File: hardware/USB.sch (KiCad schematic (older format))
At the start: 9 parts, among them IC9 FT232RL, J2 USB_A

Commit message: Working on layout
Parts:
- D11: value Tx -> TX
- D12: value Rx -> RX
- J2: value USB_A -> SERIAL; Mfr. (none) -> Wurth Elektronik; Mfr. No. (none) -> 629105150521; Mouser (none) -> 710-629105150521
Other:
- moved on the sheet: D11, D12, R6, R7
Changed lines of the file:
@@
 EESchema Schematic File Version 4
-LIBS:Sweet 6502 Computer-cache
+LIBS:Retro PC-cache
 EELAYER 30 0
 EELAYER END
@@
 AR Path="/5E9064F2/5E95D1DF" Ref="J2"  Part="1"
 F 0 "J2" H 2970 3347 50  0000 R CNN
-F 1 "USB_A" H 2970 3438 50  0000 R CNN
+F 1 "SERIAL" H 2970 3438 50  0000 R CNN
 F 2 "Connector_USB:USB_Micro-B_Wuerth_629105150521" H 3350 3400 50  0001 C CNN
 F 3 "https://www.belfuse.com/resources/datasheets/stewartconnector/ds-stw-usb-2.0-and-3.0-connectors.pdf" H 3350 3400 50  0001 C CNN
-F 4 "" H 3200 3450 50  0001 C CNN "Mfr."
-F 5 "" H 3200 3450 50  0001 C CNN "Mfr. No."
-F 6 "" H 3200 3450 50  0001 C CNN "Mouser"
+F 4 "Wurth Elektronik" H 3200 3450 50  0001 C CNN "Mfr."
+F 5 "629105150521" H 3200 3450 50  0001 C CNN "Mfr. No."
+F 6 "710-629105150521" H 3200 3450 50  0001 C CNN "Mouser"
 	1    3200 3450
 	1    0    0    -1
@@
 L Device:LED D?
 U 1 1 5E95D1E6
-P 7400 3950
+P 7400 3500
 AR Path="/5E95D1E6" Ref="D?"  Part="1"
 AR Path="/5E9064F2/5E95D1E6" Ref="D11"  Part="1"
-F 0 "D11" V 7439 3832 50  0000 R CNN
-F 1 "Tx" V 7348 3832 50  0000 R CNN
-F 2 "LED_SMD:LED_0805_2012Metric" H 7400 3950 50  0001 C CNN
-F 3 "https://www.mouser.de/datasheet/2/216/apt2012pyw-1173287.pdf" H 7400 3950 50  0001 C CNN
-F 4 "Kingbright" H 7400 3950 50  0001 C CNN "Mfr."
-F 5 "APT2012PYW" H 7400 3950 50  0001 C CNN "Mfr. No."
-F 6 "604-APT2012PYW" H 7400 3950 50  0001 C CNN "Mouser"
-	1    7400 3950
+F 0 "D11" V 7439 3382 50  0000 R CNN
+F 1 "TX" V 7348 3382 50  0000 R CNN
+F 2 "LED_SMD:LED_0805_2012Metric" H 7400 3500 50  0001 C CNN
+F 3 "https://www.mouser.de/datasheet/2/216/apt2012pyw-1173287.pdf" H 7400 3500 50  0001 C CNN
+F 4 "Kingbright" H 7400 3500 50  0001 C CNN "Mfr."
+F 5 "APT2012PYW" H 7400 3500 50  0001 C CNN "Mfr. No."
+F 6 "604-APT2012PYW" H 7400 3500 50  0001 C CNN "Mouser"
+	1    7400 3500
 	0    -1   -1   0
 $EndComp
@@
 L Device:R R?
 U 1 1 5E95D1EC
-P 7400 3600
+P 7400 3950
 AR Path="/5E95D1EC" Ref="R?"  Part="1"
 AR Path="/5E9064F2/5E95D1EC" Ref="R6"  Part="1"
-F 0 "R6" H 7470 3646 50  0000 L CNN
-F 1 "1k" H 7470 3555 50  0000 L CNN
-F 2 "Resistor_SMD:R_0805_2012Metric" V 7330 3600 50  0001 C CNN
-F 3 "~" H 7400 3600 50  0001 C CNN
-F 4 "Vishay / Dale" H 7400 3600 50  0001 C CNN "Mfr."
-F 5 "CRCW08051K00FKEAC" H 7400 3600 50  0001 C CNN "Mfr. No."
-F 6 "71-CRCW08051K00FKEAC" H 7400 3600 50  0001 C CNN "Mouser"
-	1    7400 3600
+F 0 "R6" H 7470 3996 50  0000 L CNN
+F 1 "1k" H 7470 3905 50  0000 L CNN
+F 2 "Resistor_SMD:R_0805_2012Metric" V 7330 3950 50  0001 C CNN
+F 3 "https://www.mouser.de/datasheet/2/427/crcwce3-1223726.pdf" H 7400 3950 50  0001 C CNN
+F 4 "Vishay / Dale" H 7400 3950 50  0001 C CNN "Mfr."
+F 5 "CRCW08051K00FKEAC" H 7400 3950 50  0001 C CNN "Mfr. No."
+F 6 "71-CRCW08051K00FKEAC" H 7400 3950 50  0001 C CNN "Mouser"
+	1    7400 3950
 	1    0    0    -1
 $EndComp
@@
 L Device:R R?
 U 1 1 5E95D1F2
-P 7750 3600
+P 7750 3950
 AR Path="/5E95D1F2" Ref="R?"  Part="1"
 AR Path="/5E9064F2/5E95D1F2" Ref="R7"  Part="1"
-F 0 "R7" H 7820 3646 50  0000 L CNN
-F 1 "1k" H 7820 3555 50  0000 L CNN
-F 2 "Resistor_SMD:R_0805_2012Metric" V 7680 3600 50  0001 C CNN
-F 3 "~" H 7750 3600 50  0001 C CNN
-F 4 "Vishay / Dale" H 7750 3600 50  0001 C CNN "Mfr."
-F 5 "CRCW08051K00FKEAC" H 7750 3600 50  0001 C CNN "Mfr. No."
-F 6 "71-CRCW08051K00FKEAC" H 7750 3600 50  0001 C CNN "Mouser"
-	1    7750 3600
+F 0 "R7" H 7820 3996 50  0000 L CNN
+F 1 "1k" H 7820 3905 50  0000 L CNN
+F 2 "Resistor_SMD:R_0805_2012Metric" V 7680 3950 50  0001 C CNN
+F 3 "https://www.mouser.de/datasheet/2/427/crcwce3-1223726.pdf" H 7750 3950 50  0001 C CNN
+F 4 "Vishay / Dale" H 7750 3950 50  0001 C CNN "Mfr."
+F 5 "CRCW08051K00FKEAC" H 7750 3950 50  0001 C CNN "Mfr. No."
+F 6 "71-CRCW08051K00FKEAC" H 7750 3950 50  0001 C CNN "Mouser"
+	1    7750 3950
 	1    0    0    -1
 $EndComp
@@
 L Device:LED D?
 U 1 1 5E95D1F8
-P 7750 3950
+P 7750 3500
 AR Path="/5E95D1F8" Ref="D?"  Part="1"
 AR Path="/5E9064F2/5E95D1F8" Ref="D12"  Part="1"
-F 0 "D12" V 7789 3832 50  0000 R CNN
-F 1 "Rx" V 7698 3832 50  0000 R CNN
-F 2 "LED_SMD:LED_0805_2012Metric" H 7750 3950 50  0001 C CNN
-F 3 "https://www.mouser.de/datasheet/2/216/apt2012pgw-1173286.pdf" H 7750 3950 50  0001 C CNN
-F 4 "Kingbright" H 7750 3950 50  0001 C CNN "Mfr."
-F 5 "APT2012PGW" H 7750 3950 50  0001 C CNN "Mfr. No."
-F 6 "604-APT2012PGW" H 7750 3950 50  0001 C CNN "Mouser"
-	1    7750 3950
+F 0 "D12" V 7789 3382 50  0000 R CNN
+F 1 "RX" V 7698 3382 50  0000 R CNN
+F 2 "LED_SMD:LED_0805_2012Metric" H 7750 3500 50  0001 C CNN
+F 3 "https://www.mouser.de/datasheet/2/216/apt2012pgw-1173286.pdf" H 7750 3500 50  0001 C CNN
+F 4 "Kingbright" H 7750 3500 50  0001 C CNN "Mfr."
+F 5 "APT2012PGW" H 7750 3500 50  0001 C CNN "Mfr. No."
+F 6 "604-APT2012PGW" H 7750 3500 50  0001 C CNN "Mouser"
+	1    7750 3500
 	0    -1   -1   0
 $EndComp
@@
 F 1 "100nF" H 4515 3105 50  0000 L CNN
 F 2 "Capacitor_SMD:C_0805_2012Metric" H 4438 3000 50  0001 C CNN
-F 3 "~" H 4400 3150 50  0001 C CNN
+F 3 "https://www.mouser.de/datasheet/2/212/KEM_C1002_X7R_SMD-1102033.pdf" H 4400 3150 50  0001 C CNN
 F 4 "KEMET" H 4400 3150 50  0001 C CNN "Mfr."
 F 5 "C0805C104K5RACTU" H 4400 3150 50  0001 C CNN "Mfr. No."
@@
 	7600 3300 7400 3300
 Wire Wire Line
-	7400 3300 7400 3450
-Wire Wire Line
 	7600 3300 7750 3300
-Wire Wire Line
-	7750 3300 7750 3450
 Connection ~ 7600 3300
 Wire Wire Line
-	7750 3750 7750 3800
-Wire Wire Line
-	7400 3750 7400 3800
-Wire Wire Line
 	6450 4150 7400 4150
 Wire Wire Line
-	7400 4150 7400 4100
-Wire Wire Line
 	6450 4250 7750 4250
 Wire Wire Line
-	7750 4250 7750 4100
+	7750 3800 7750 3650
 Wire Wire Line
 	4750 3850 4850 3850
@@
 F 1 "100nF" H 5265 2355 50  0000 L CNN
 F 2 "Capacitor_SMD:C_0805_2012Metric" H 5188 2250 50  0001 C CNN
-F 3 "~" H 5150 2400 50  0001 C CNN
+F 3 "https://www.mouser.de/datasheet/2/212/KEM_C1002_X7R_SMD-1102033.pdf" H 5150 2400 50  0001 C CNN
 F 4 "KEMET" H 5150 2400 50  0001 C CNN "Mfr."
 F 5 "C0805C104K5RACTU" H 5150 2400 50  0001 C CNN "Mfr. No."
@@
 F 1 "100nF" H 6065 2355 50  0000 L CNN
 F 2 "Capacitor_SMD:C_0805_2012Metric" H 5988 2250 50  0001 C CNN
-F 3 "~" H 5950 2400 50  0001 C CNN
+F 3 "https://www.mouser.de/datasheet/2/212/KEM_C1002_X7R_SMD-1102033.pdf" H 5950 2400 50  0001 C CNN
 F 4 "KEMET" H 5950 2400 50  0001 C CNN "Mfr."
 F 5 "C0805C104K5RACTU" H 5950 2400 50  0001 C CNN "Mfr. No."
@@
 	5750 2000 5750 2100
 Connection ~ 5750 2100
+Wire Wire Line
+	7400 4100 7400 4150
+Wire Wire Line
+	7750 4100 7750 4250
+Wire Wire Line
+	7400 3650 7400 3800
+Wire Wire Line
+	7400 3350 7400 3300
+Wire Wire Line
+	7750 3350 7750 3300
 $EndSCHEMATC

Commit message: Working on layout
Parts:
- J2: footprint Connector_USB:USB_Micro-B_Wuerth_629105150521 -> Connector_USB:USB_B_TE_5787834_Vertical; Mfr. Wurth Elektronik -> TE Connectivity; Mfr. No. 629105150521 -> 5787834-1; Mouser 710-629105150521 -> 571-5787834-1
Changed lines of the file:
@@
 $Descr A4 11693 8268
 encoding utf-8
-Sheet 4 6
+Sheet 3 6
 Title "Retro PC"
 Date "2019-10-08"
@@
 F 0 "J2" H 2970 3347 50  0000 R CNN
 F 1 "SERIAL" H 2970 3438 50  0000 R CNN
-F 2 "Connector_USB:USB_Micro-B_Wuerth_629105150521" H 3350 3400 50  0001 C CNN
+F 2 "Connector_USB:USB_B_TE_5787834_Vertical" H 3350 3400 50  0001 C CNN
 F 3 "https://www.belfuse.com/resources/datasheets/stewartconnector/ds-stw-usb-2.0-and-3.0-connectors.pdf" H 3350 3400 50  0001 C CNN
-F 4 "Wurth Elektronik" H 3200 3450 50  0001 C CNN "Mfr."
-F 5 "629105150521" H 3200 3450 50  0001 C CNN "Mfr. No."
-F 6 "710-629105150521" H 3200 3450 50  0001 C CNN "Mouser"
+F 4 "TE Connectivity" H 3200 3450 50  0001 C CNN "Mfr."
+F 5 "5787834-1" H 3200 3450 50  0001 C CNN "Mfr. No."
+F 6 "571-5787834-1" H 3200 3450 50  0001 C CNN "Mouser"
 	1    3200 3450
 	1    0    0    -1

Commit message: Working on layout
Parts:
- J2: footprint Connector_USB:USB_B_TE_5787834_Vertical -> TE_Connectivity:USB_B_TE_2923042_Horizontal; Mfr. No. 5787834-1 -> 292304-2; Mouser 571-5787834-1 -> 571-292304-2
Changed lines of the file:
@@
 F 0 "J2" H 2970 3347 50  0000 R CNN
 F 1 "SERIAL" H 2970 3438 50  0000 R CNN
-F 2 "Connector_USB:USB_B_TE_5787834_Vertical" H 3350 3400 50  0001 C CNN
-F 3 "https://www.belfuse.com/resources/datasheets/stewartconnector/ds-stw-usb-2.0-and-3.0-connectors.pdf" H 3350 3400 50  0001 C CNN
+F 2 "TE_Connectivity:USB_B_TE_2923042_Horizontal" H 3350 3400 50  0001 C CNN
+F 3 "https://www.te.com/commerce/DocumentDelivery/DDEController?Action=showdoc&DocId=Customer+Drawing%7F292304%7FD4%7Fpdf%7FEnglish%7FENG_CD_292304_D4.pdf%7F292304-2" H 3350 3400 50  0001 C CNN
 F 4 "TE Connectivity" H 3200 3450 50  0001 C CNN "Mfr."
-F 5 "5787834-1" H 3200 3450 50  0001 C CNN "Mfr. No."
-F 6 "571-5787834-1" H 3200 3450 50  0001 C CNN "Mouser"
+F 5 "292304-2" H 3200 3450 50  0001 C CNN "Mfr. No."
+F 6 "571-292304-2" H 3200 3450 50  0001 C CNN "Mouser"
 	1    3200 3450
 	1    0    0    -1

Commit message: Working on layout
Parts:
- removed J2: SERIAL, TE_Connectivity:USB_B_TE_2923042_Horizontal, symbol Connector:USB_A
- added J1: USB_B, TE_Connectivity:USB_B_TE_2923042_Horizontal, symbol TE_Connectivity:USB_B
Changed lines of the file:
@@
-$EndComp
-$Comp
-L Connector:USB_A J?
-U 1 1 5E95D1DF
-P 3200 3450
-AR Path="/5E95D1DF" Ref="J?"  Part="1"
-AR Path="/5E9064F2/5E95D1DF" Ref="J2"  Part="1"
-F 0 "J2" H 2970 3347 50  0000 R CNN
-F 1 "SERIAL" H 2970 3438 50  0000 R CNN
-F 2 "TE_Connectivity:USB_B_TE_2923042_Horizontal" H 3350 3400 50  0001 C CNN
-F 3 "https://www.te.com/commerce/DocumentDelivery/DDEController?Action=showdoc&DocId=Customer+Drawing%7F292304%7FD4%7Fpdf%7FEnglish%7FENG_CD_292304_D4.pdf%7F292304-2" H 3350 3400 50  0001 C CNN
-F 4 "TE Connectivity" H 3200 3450 50  0001 C CNN "Mfr."
-F 5 "292304-2" H 3200 3450 50  0001 C CNN "Mfr. No."
-F 6 "571-292304-2" H 3200 3450 50  0001 C CNN "Mouser"
-	1    3200 3450
-	1    0    0    -1
 $EndComp
 $Comp
@@
 Wire Wire Line
 	7750 3350 7750 3300
+$Comp
+L TE_Connectivity:USB_B J1
+U 1 1 5DA7E5BF
+P 3200 3450
+F 0 "J1" H 3257 3917 50  0000 C CNN
+F 1 "USB_B" H 3257 3826 50  0000 C CNN
+F 2 "TE_Connectivity:USB_B_TE_2923042_Horizontal" H 3350 3400 50  0001 C CNN
+F 3 "https://www.te.com/commerce/DocumentDelivery/DDEController?Action=showdoc&DocId=Customer+Drawing%7F292304%7FD4%7Fpdf%7FEnglish%7FENG_CD_292304_D4.pdf%7F292304-2" H 3350 3400 50  0001 C CNN
+F 4 "TE Connectivity" H 3257 4007 50  0001 C CNN "Mfr."
+F 5 "292304-2" H 3257 3916 50  0001 C CNN "Mfr. No."
+F 6 "571-292304-2" H 3257 3825 50  0001 C CNN "Mouser"
+	1    3200 3450
+	1    0    0    -1
+$EndComp
 $EndSCHEMATC

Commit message: Working on layout
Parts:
- X2: renamed from J1; footprint TE_Connectivity:USB_B_TE_2923042_Horizontal -> Connector_Custom:USB-B_TE_2923042_Horizontal; symbol TE_Connectivity:USB_B -> Connector_Custom:USB-B
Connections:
- net labels added: ~ModemReady
- net labels removed: ModemReady
- wire segments 45 -> 43
- no-connect marks 9 -> 10
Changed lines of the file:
@@
 $Descr A4 11693 8268
 encoding utf-8
-Sheet 3 6
+Sheet 6 6
 Title "Retro PC"
 Date "2019-10-08"
@@
 	1    0    0    -1
 $EndComp
-$Comp
-L power:+5V #PWR?
-U 1 1 5ECF32B5
-P 3600 3200
-AR Path="/5ECF32B5" Ref="#PWR?"  Part="1"
-AR Path="/5E9064F2/5ECF32B5" Ref="#PWR048"  Part="1"
-F 0 "#PWR048" H 3600 3050 50  0001 C CNN
-F 1 "+5V" H 3615 3373 50  0000 C CNN
-F 2 "" H 3600 3200 50  0001 C CNN
-F 3 "" H 3600 3200 50  0001 C CNN
-	1    3600 3200
-	1    0    0    -1
-$EndComp
-Wire Wire Line
-	3500 3250 3600 3250
-Wire Wire Line
-	3600 3250 3600 3200
 Text HLabel 4750 3850 0    50   Input ~ 0
 ~RESET
@@
 	6600 3450 6450 3450
 Text HLabel 6600 3550 2    50   Output ~ 0
-ModemReady
+~ModemReady
 Wire Wire Line
 	6450 3550 6600 3550
@@
 	7750 3350 7750 3300
 $Comp
-L TE_Connectivity:USB_B J1
+L Connector_Custom:USB-B X2
 U 1 1 5DA7E5BF
 P 3200 3450
-F 0 "J1" H 3257 3917 50  0000 C CNN
+AR Path="/5DA7E5BF" Ref="X2"  Part="1"
+AR Path="/5E9064F2/5DA7E5BF" Ref="X2"  Part="1"
+F 0 "X2" H 3257 3917 50  0000 C CNN
 F 1 "USB_B" H 3257 3826 50  0000 C CNN
-F 2 "TE_Connectivity:USB_B_TE_2923042_Horizontal" H 3350 3400 50  0001 C CNN
+F 2 "Connector_Custom:USB-B_TE_2923042_Horizontal" H 3350 3400 50  0001 C CNN
 F 3 "https://www.te.com/commerce/DocumentDelivery/DDEController?Action=showdoc&DocId=Customer+Drawing%7F292304%7FD4%7Fpdf%7FEnglish%7FENG_CD_292304_D4.pdf%7F292304-2" H 3350 3400 50  0001 C CNN
 F 4 "TE Connectivity" H 3257 4007 50  0001 C CNN "Mfr."
@@
 	1    0    0    -1
 $EndComp
+NoConn ~ 3500 3250
 $EndSCHEMATC

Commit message: First version of the layout
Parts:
- R6, R7: Mfr. Vishay / Dale -> Yageo; Mfr. No. CRCW08051K00FKEAC -> MFP-25BRD52-1K; Mouser 71-CRCW08051K00FKEAC -> 603-MFP-25BRD52-1K
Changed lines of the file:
@@
 F 1 "1k" H 7470 3905 50  0000 L CNN
 F 2 "Resistor_SMD:R_0805_2012Metric" V 7330 3950 50  0001 C CNN
-F 3 "https://www.mouser.de/datasheet/2/427/crcwce3-1223726.pdf" H 7400 3950 50  0001 C CNN
-F 4 "Vishay / Dale" H 7400 3950 50  0001 C CNN "Mfr."
-F 5 "CRCW08051K00FKEAC" H 7400 3950 50  0001 C CNN "Mfr. No."
-F 6 "71-CRCW08051K00FKEAC" H 7400 3950 50  0001 C CNN "Mouser"
+F 3 "https://www.mouser.de/datasheet/2/447/Yageo%20LR_MFP_2013-594635.pdf" H 7400 3950 50  0001 C CNN
+F 4 "Yageo" H 7400 3950 50  0001 C CNN "Mfr."
+F 5 "MFP-25BRD52-1K" H 7400 3950 50  0001 C CNN "Mfr. No."
+F 6 "603-MFP-25BRD52-1K" H 7400 3950 50  0001 C CNN "Mouser"
 	1    7400 3950
 	1    0    0    -1
@@
 F 1 "1k" H 7820 3905 50  0000 L CNN
 F 2 "Resistor_SMD:R_0805_2012Metric" V 7680 3950 50  0001 C CNN
-F 3 "https://www.mouser.de/datasheet/2/427/crcwce3-1223726.pdf" H 7750 3950 50  0001 C CNN
-F 4 "Vishay / Dale" H 7750 3950 50  0001 C CNN "Mfr."
-F 5 "CRCW08051K00FKEAC" H 7750 3950 50  0001 C CNN "Mfr. No."
-F 6 "71-CRCW08051K00FKEAC" H 7750 3950 50  0001 C CNN "Mouser"
+F 3 "https://www.mouser.de/datasheet/2/447/Yageo%20LR_MFP_2013-594635.pdf" H 7750 3950 50  0001 C CNN
+F 4 "Yageo" H 7750 3950 50  0001 C CNN "Mfr."
+F 5 "MFP-25BRD52-1K" H 7750 3950 50  0001 C CNN "Mfr. No."
+F 6 "603-MFP-25BRD52-1K" H 7750 3950 50  0001 C CNN "Mouser"
 	1    7750 3950
 	1    0    0    -1

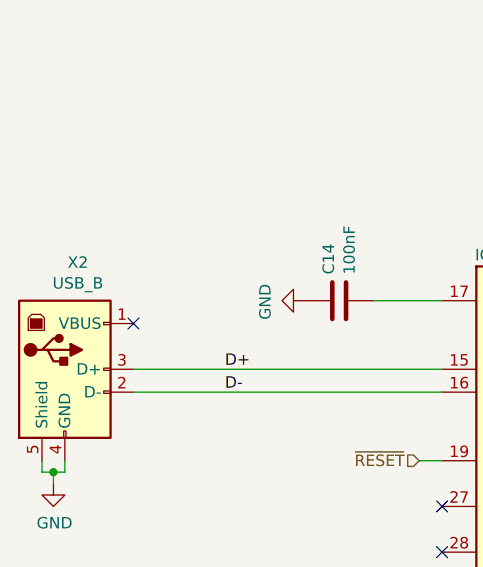
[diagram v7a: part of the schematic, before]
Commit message: Replace LCD
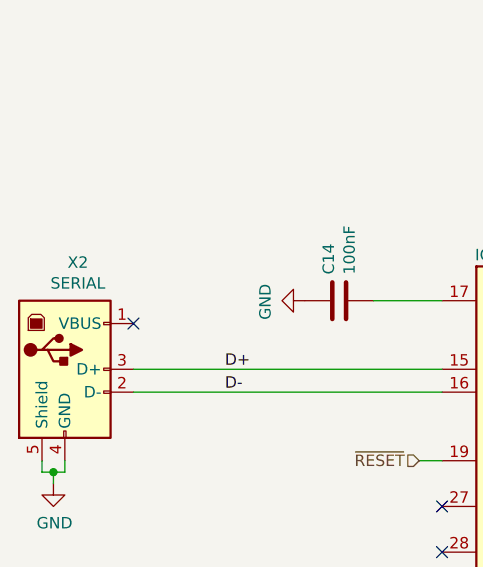
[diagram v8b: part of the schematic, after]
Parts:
- X2: value USB_B -> SERIAL
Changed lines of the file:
@@
 AR Path="/5E9064F2/5DA7E5BF" Ref="X2"  Part="1"
 F 0 "X2" H 3257 3917 50  0000 C CNN
-F 1 "USB_B" H 3257 3826 50  0000 C CNN
+F 1 "SERIAL" H 3257 3826 50  0000 C CNN
 F 2 "Connector_Custom:USB-B_TE_2923042_Horizontal" H 3350 3400 50  0001 C CNN
 F 3 "https://www.te.com/commerce/DocumentDelivery/DDEController?Action=showdoc&DocId=Customer+Drawing%7F292304%7FD4%7Fpdf%7FEnglish%7FENG_CD_292304_D4.pdf%7F292304-2" H 3350 3400 50  0001 C CNN
